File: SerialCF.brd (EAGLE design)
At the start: 106.7 x 50.5 mm, 18 parts, among them IC1 XR-16C550P, T1 BC547, T2 BC547

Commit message: Update SerialCF Picture
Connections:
- net GND: now also V3.4; no longer V3.6
- net VCC: now also V3.6; no longer V3.4
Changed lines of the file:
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@@
 <contactref element="C4" pad="1"/>
 <contactref element="V3" pad="16"/>
-<contactref element="V3" pad="4"/>
 <contactref element="R6" pad="2"/>
 <polygon width="0.4064" layer="1" isolate="0.3048">
@@
 <vertex x="105.41" y="49.53"/>
 </polygon>
+<contactref element="V3" pad="6"/>
+<wire x1="19.78" y1="48.53" x2="19.722940625" y2="48.66775625" width="0.254" layer="1"/>
+<wire x1="70.61" y1="46.92" x2="70.614990625" y2="46.939196875" width="0.254" layer="1"/>
 <wire x1="78.74" y1="39.37" x2="65.405" y2="30.48" width="0" layer="19" extent="1-1"/>
 <wire x1="58.42" y1="11.43" x2="69.85" y2="12.065" width="0" layer="19" extent="1-1"/>
@@
 <contactref element="C4" pad="2"/>
 <contactref element="V3" pad="8"/>
-<contactref element="V3" pad="6"/>
 <contactref element="T2" pad="1"/>
 <contactref element="JP1" pad="2"/>
@@
 <contactref element="JP1" pad="78"/>
 <contactref element="JP1" pad="80"/>
+<contactref element="V3" pad="4"/>
 </signal>
 <signal name="A0">

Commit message: Use upper Bits to Address IO devices.
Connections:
- net A10: now also V3.3
- net A11: now also V3.6
- net A5: no longer V3.1
- net A6: no longer V3.2
- net A7: no longer V3.3
- net A8: now also V3.1
- net A9: now also V3.2
- net VCC: no longer V3.6
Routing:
- net A8: track 0.00 -> 175.3 mm, vias 0 -> 4
- net A9: track 0.00 -> 97.7 mm, vias 0 -> 2
- net A10: track 0.00 -> 94.6 mm, vias 0 -> 3
- net A11: track 0.00 -> 70.6 mm, vias 0 -> 3

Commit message: Use LS version for serialCF
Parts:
- removed V3: 74138N, 74ttl-din:DIL16
- added IC2: 74LS138N, 74xx-eu:DIL16
- moved C2 2.54 mm to (5.08, 40.6)
- moved C4 2.54 mm to (81.3, 36.8)
- moved SV1 1.27 mm to (38.1, 43.2)
- moved SV2 1.27 mm to (72.4, 43.2)
- moved R1 1.27 mm to (39.4, 38.1)
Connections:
- net A10: now also IC2.3; no longer V3.3
- net A11: now also IC2.6; no longer V3.6
- net A8: now also IC2.1; no longer V3.1
- net A9: now also IC2.2; no longer V3.2
- net GND: now also IC2.8; no longer V3.4, V3.8
- net IOCS1: no longer V3.15
- net N$4: now also IC2.14; no longer V3.14
- net N$5: no longer V3.5
- net VCC: now also IC2.16; no longer V3.16
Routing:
- net A5: track 116.7 -> 0.00 mm, vias 2 -> 0
- net A7: track 108.0 -> 0.00 mm, vias 1 -> 0
- net A6: track 90.3 -> 0.00 mm, vias 2 -> 0
- net IOCS1: track 87.6 -> 0.00 mm
- net A8: track 175.3 -> 100.5 mm, vias 4 -> 0
- net N$5: track 59.7 -> 0.00 mm
- net A10: track 94.6 -> 65.2 mm, vias 3 -> 0
- net A9: track 97.7 -> 69.5 mm, vias 2 -> 1
- net A2: track 113.1 -> 136.3 mm, vias 1 -> 0
- net !RD: track 85.4 -> 102.9 mm
- net A11: track 70.6 -> 53.2 mm, vias 3 -> 1
- net N$9: track 84.6 -> 74.2 mm
- net WAIT: track 88.2 -> 79.1 mm, vias 1 -> 3
- net !WR: track 77.2 -> 68.4 mm
- net !RESET: track 77.8 -> 69.3 mm
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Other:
- board size 106.7 x 50.5 mm -> 106.7 x 49.2 mm

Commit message: Update SerialCF
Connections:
- net A11: now also IC2.4; no longer IC2.6
- net GND: now also IC2.6
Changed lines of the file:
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@@
 <contactref element="JP1" pad="80"/>
 <contactref element="IC2" pad="8"/>
+<contactref element="IC2" pad="6"/>
+<wire x1="83.82" y1="44.45" x2="96.52" y2="44.45" width="0" layer="19" extent="1-1"/>
+<wire x1="78.74" y1="44.45" x2="83.82" y2="44.45" width="0" layer="19" extent="1-1"/>
+<wire x1="76.2" y1="44.45" x2="78.74" y2="44.45" width="0" layer="19" extent="1-1"/>
+<wire x1="73.66" y1="44.45" x2="76.2" y2="44.45" width="0" layer="19" extent="1-1"/>
+<wire x1="71.12" y1="41.91" x2="73.66" y2="44.45" width="0" layer="19" extent="1-1"/>
+<wire x1="83.82" y1="36.83" x2="83.82" y2="44.45" width="0" layer="19" extent="1-1"/>
+<wire x1="73.66" y1="30.48" x2="71.12" y2="41.91" width="0" layer="19" extent="1-1"/>
+<wire x1="72.39" y1="17.78" x2="73.66" y2="30.48" width="0" layer="19" extent="1-1"/>
+<wire x1="72.39" y1="3.81" x2="72.39" y2="17.78" width="0" layer="19" extent="1-1"/>
+<wire x1="74.93" y1="3.81" x2="72.39" y2="3.81" width="0" layer="19" extent="1-1"/>
+<wire x1="77.47" y1="3.81" x2="74.93" y2="3.81" width="0" layer="19" extent="1-1"/>
+<wire x1="80.01" y1="3.81" x2="77.47" y2="3.81" width="0" layer="19" extent="1-1"/>
+<wire x1="82.55" y1="3.81" x2="80.01" y2="3.81" width="0" layer="19" extent="1-1"/>
+<wire x1="82.55" y1="6.35" x2="82.55" y2="3.81" width="0" layer="19" extent="1-1"/>
+<wire x1="85.09" y1="3.81" x2="82.55" y2="3.81" width="0" layer="19" extent="1-1"/>
+<wire x1="87.63" y1="3.81" x2="85.09" y2="3.81" width="0" layer="19" extent="1-1"/>
+<wire x1="90.17" y1="3.81" x2="87.63" y2="3.81" width="0" layer="19" extent="1-1"/>
+<wire x1="92.71" y1="3.81" x2="90.17" y2="3.81" width="0" layer="19" extent="1-1"/>
+<wire x1="95.25" y1="3.81" x2="92.71" y2="3.81" width="0" layer="19" extent="1-1"/>
+<wire x1="97.79" y1="3.81" x2="95.25" y2="3.81" width="0" layer="19" extent="1-1"/>
+<wire x1="100.33" y1="3.81" x2="97.79" y2="3.81" width="0" layer="19" extent="1-1"/>
+<wire x1="102.87" y1="3.81" x2="100.33" y2="3.81" width="0" layer="19" extent="1-1"/>
+<wire x1="69.85" y1="3.81" x2="72.39" y2="3.81" width="0" layer="19" extent="1-1"/>
+<wire x1="67.31" y1="3.81" x2="69.85" y2="3.81" width="0" layer="19" extent="1-1"/>
+<wire x1="64.77" y1="3.81" x2="67.31" y2="3.81" width="0" layer="19" extent="1-1"/>
+<wire x1="62.23" y1="3.81" x2="64.77" y2="3.81" width="0" layer="19" extent="1-1"/>
+<wire x1="59.69" y1="3.81" x2="62.23" y2="3.81" width="0" layer="19" extent="1-1"/>
+<wire x1="57.15" y1="3.81" x2="59.69" y2="3.81" width="0" layer="19" extent="1-1"/>
+<wire x1="54.61" y1="3.81" x2="57.15" y2="3.81" width="0" layer="19" extent="1-1"/>
+<wire x1="52.07" y1="3.81" x2="54.61" y2="3.81" width="0" layer="19" extent="1-1"/>
+<wire x1="49.53" y1="3.81" x2="52.07" y2="3.81" width="0" layer="19" extent="1-1"/>
+<wire x1="46.99" y1="3.81" x2="49.53" y2="3.81" width="0" layer="19" extent="1-1"/>
+<wire x1="44.45" y1="3.81" x2="46.99" y2="3.81" width="0" layer="19" extent="1-1"/>
+<wire x1="41.91" y1="3.81" x2="44.45" y2="3.81" width="0" layer="19" extent="1-1"/>
+<wire x1="39.37" y1="3.81" x2="41.91" y2="3.81" width="0" layer="19" extent="1-1"/>
+<wire x1="39.37" y1="6.35" x2="39.37" y2="3.81" width="0" layer="19" extent="1-1"/>
+<wire x1="36.83" y1="3.81" x2="39.37" y2="3.81" width="0" layer="19" extent="1-1"/>
+<wire x1="34.29" y1="3.81" x2="36.83" y2="3.81" width="0" layer="19" extent="1-1"/>
+<wire x1="31.75" y1="3.81" x2="34.29" y2="3.81" width="0" layer="19" extent="1-1"/>
+<wire x1="29.21" y1="3.81" x2="31.75" y2="3.81" width="0" layer="19" extent="1-1"/>
+<wire x1="26.67" y1="3.81" x2="29.21" y2="3.81" width="0" layer="19" extent="1-1"/>
+<wire x1="24.13" y1="3.81" x2="26.67" y2="3.81" width="0" layer="19" extent="1-1"/>
+<wire x1="21.59" y1="3.81" x2="24.13" y2="3.81" width="0" layer="19" extent="1-1"/>
+<wire x1="19.05" y1="3.81" x2="21.59" y2="3.81" width="0" layer="19" extent="1-1"/>
+<wire x1="16.51" y1="3.81" x2="19.05" y2="3.81" width="0" layer="19" extent="1-1"/>
+<wire x1="13.97" y1="3.81" x2="16.51" y2="3.81" width="0" layer="19" extent="1-1"/>
+<wire x1="11.43" y1="3.81" x2="13.97" y2="3.81" width="0" layer="19" extent="1-1"/>
+<wire x1="8.89" y1="3.81" x2="11.43" y2="3.81" width="0" layer="19" extent="1-1"/>
+<wire x1="6.35" y1="3.81" x2="8.89" y2="3.81" width="0" layer="19" extent="1-1"/>
+<wire x1="3.81" y1="3.81" x2="6.35" y2="3.81" width="0" layer="19" extent="1-1"/>
+<wire x1="20.32" y1="11.43" x2="21.59" y2="3.81" width="0" layer="19" extent="1-1"/>
+<wire x1="12.7" y1="11.43" x2="20.32" y2="11.43" width="0" layer="19" extent="1-1"/>
+<wire x1="6.35" y1="16.51" x2="12.7" y2="11.43" width="0" layer="19" extent="1-1"/>
+<wire x1="10.16" y1="26.67" x2="6.35" y2="16.51" width="0" layer="19" extent="1-1"/>
+<wire x1="12.7" y1="26.67" x2="10.16" y2="26.67" width="0" layer="19" extent="1-1"/>
+<wire x1="5.08" y1="38.1" x2="10.16" y2="26.67" width="0" layer="19" extent="1-1"/>
+<wire x1="22.86" y1="36.83" x2="12.7" y2="26.67" width="0" layer="19" extent="1-1"/>
+<wire x1="27.94" y1="36.83" x2="22.86" y2="36.83" width="0" layer="19" extent="1-1"/>
+<wire x1="41.91" y1="43.18" x2="27.94" y2="36.83" width="0" layer="19" extent="1-1"/>
+<wire x1="48.26" y1="44.45" x2="41.91" y2="43.18" width="0" layer="19" extent="1-1"/>
 </signal>
 <signal name="A0">
@@
 <signal name="A11">
 <contactref element="JP1" pad="41"/>
-<contactref element="IC2" pad="6"/>
 <wire x1="23" y1="35.42" x2="23" y2="36.8" width="0.254" layer="1"/>
 <wire x1="24.15" y1="34.27" x2="23" y2="35.42" width="0.254" layer="1"/>
@@
 <wire x1="49.68" y1="8.97" x2="49.68" y2="9.2" width="0.254" layer="16"/>
 <wire x1="52.21" y1="6.44" x2="49.68" y2="8.97" width="0.254" layer="16"/>
-<wire x1="23" y1="36.8" x2="22.86" y2="36.83" width="0.254" layer="1"/>
 <wire x1="52.21" y1="6.44" x2="52.07" y2="6.35" width="0.254" layer="16"/>
 <via x="40.94" y="23" extent="1-16" drill="0.6096"/>
+<contactref element="IC2" pad="4"/>
+<wire x1="23" y1="36.8" x2="17.78" y2="36.83" width="0" layer="19" extent="1-1"/>
 </signal>
 <signal name="A12">

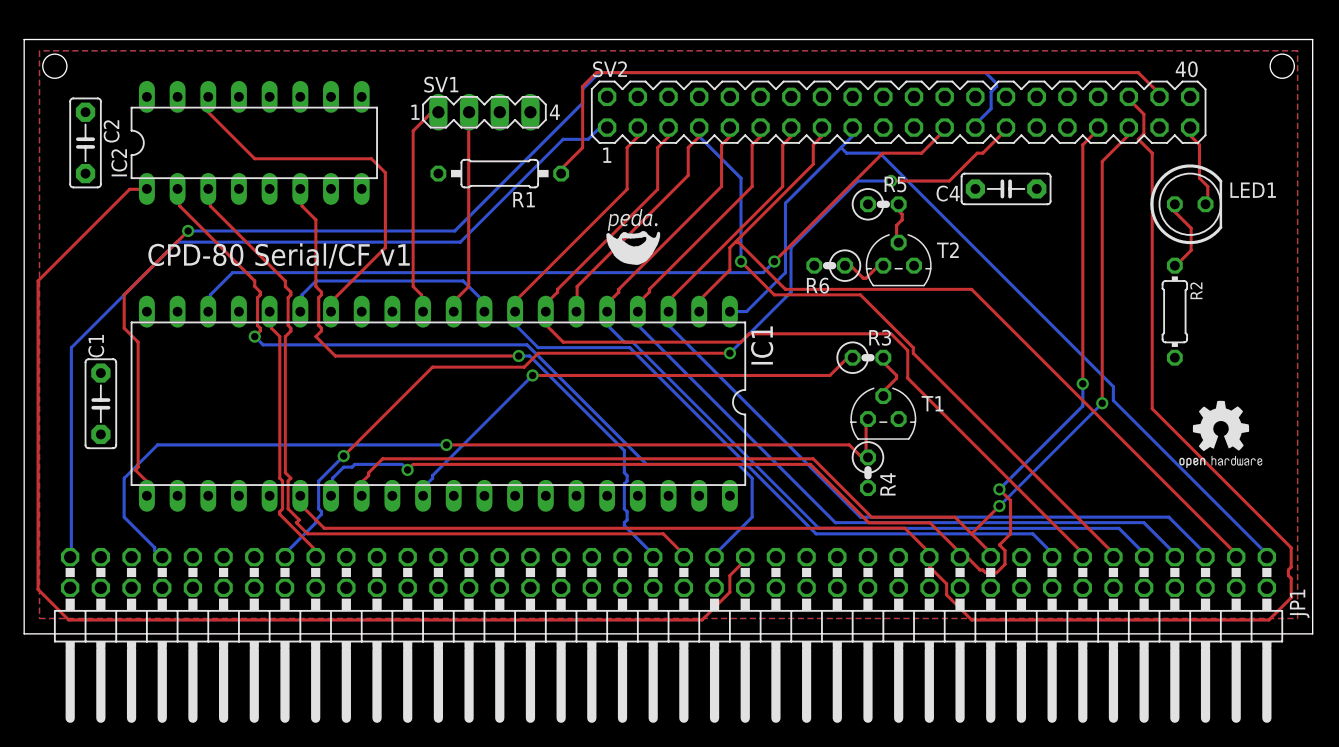
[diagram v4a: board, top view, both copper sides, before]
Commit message: Added Oscillator to SerialCF Board. And more Serial Pins
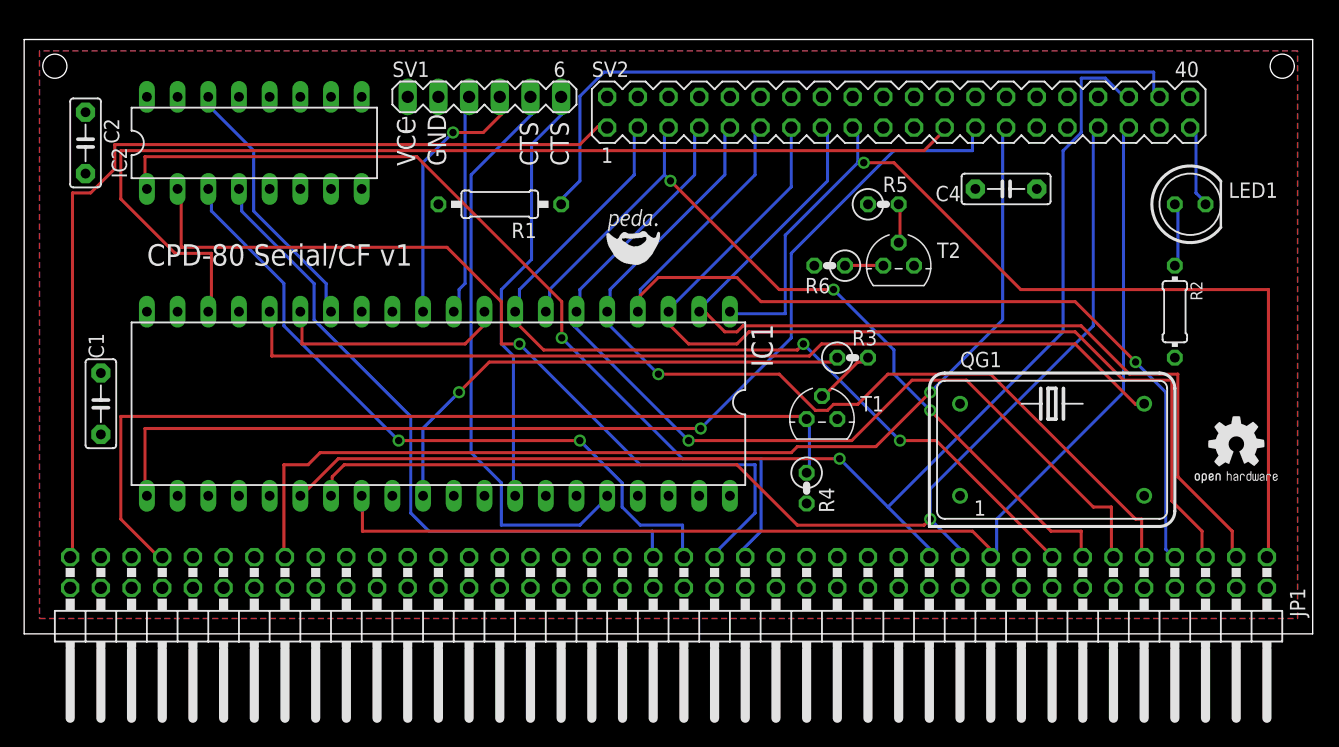
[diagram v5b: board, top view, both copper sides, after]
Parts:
- added QG1: 1.84MHz, crystal:DIL14S
- SV1: device con-lstb:MA04-1 -> con-lstb:MA06-1
- moved R4 5.24 mm to (64.8, 12.1)
- moved T1 5.08 mm to (66.0, 17.8)
- moved R1 2.54 mm to (39.4, 35.6)
- moved U$1 1.80 mm to (96.5, 11.4)
- moved SV1 1.27 mm to (38.1, 44.5)
- moved R3 1.27 mm to (68.6, 22.9)
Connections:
- new net N$12: IC1.36, SV1.5
- new net N$14: IC1.33, SV1.6
- net GND: now also QG1.7, SV1.2; no longer SV1.4
- net N$1: now also QG1.8; no longer JP1.63
- net N$11: now also SV1.4; no longer SV1.1
- net N$15: now also SV1.3; no longer SV1.2
- net VCC: now also QG1.14, SV1.1; no longer SV1.3
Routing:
- net N$1: track 22.1 -> 78.4 mm
- net N$12: track 0.00 -> 48.4 mm
- net N$14: track 0.00 -> 35.6 mm
- net A2: track 136.3 -> 103.9 mm, vias 0 -> 1
- net A8: track 100.5 -> 74.7 mm, vias 0 -> 1
- net !WR: track 68.4 -> 87.4 mm, vias 1 -> 0
- net !RD: track 102.9 -> 89.8 mm
- net D0: track 70.4 -> 83.3 mm, vias 0 -> 1
- net D3: track 73.1 -> 82.9 mm, vias 0 -> 1
- net N$4: track 31.5 -> 22.0 mm
- net WAIT: track 79.1 -> 88.1 mm, vias 3 -> 1
- net !RESET: track 69.3 -> 78.0 mm
- net D2: track 73.1 -> 80.7 mm
- net A10: track 65.2 -> 57.6 mm, vias 0 -> 2
- net D1: track 71.8 -> 79.2 mm
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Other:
- board text added: "CTS"
- board text added: "GND"
- board text added: "VCC"
- board text removed: "+"
- board text removed: "-"
